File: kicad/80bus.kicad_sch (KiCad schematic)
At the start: 9 parts, among them IC2 4049

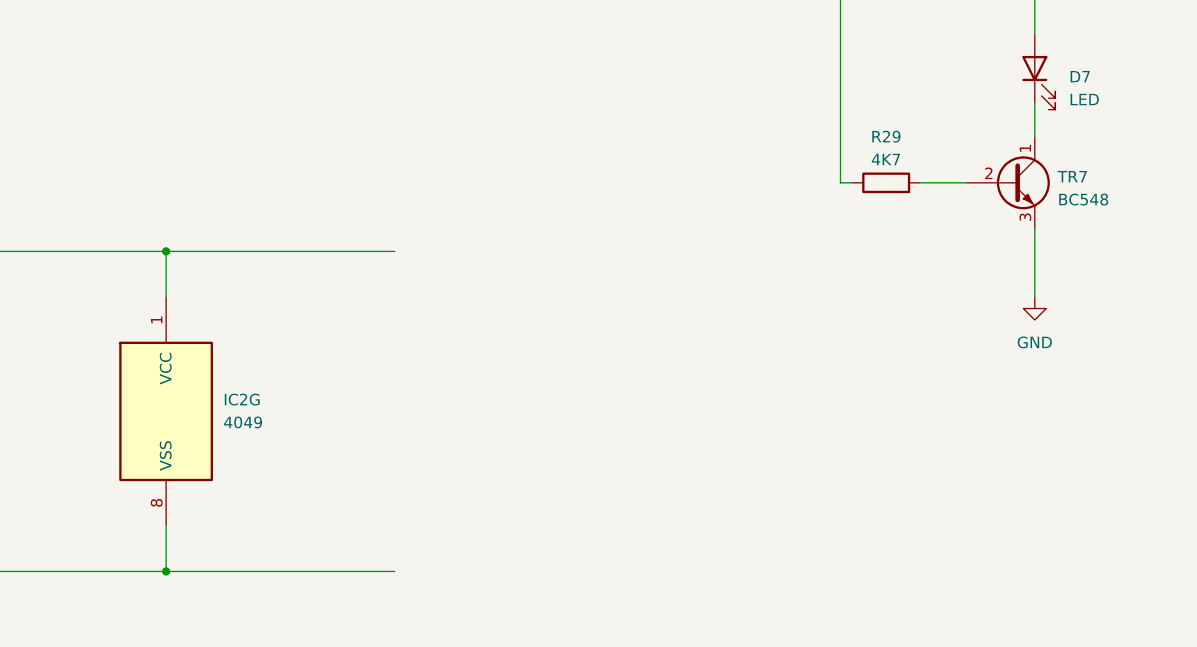
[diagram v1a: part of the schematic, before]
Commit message: Kicad 9 and Docs
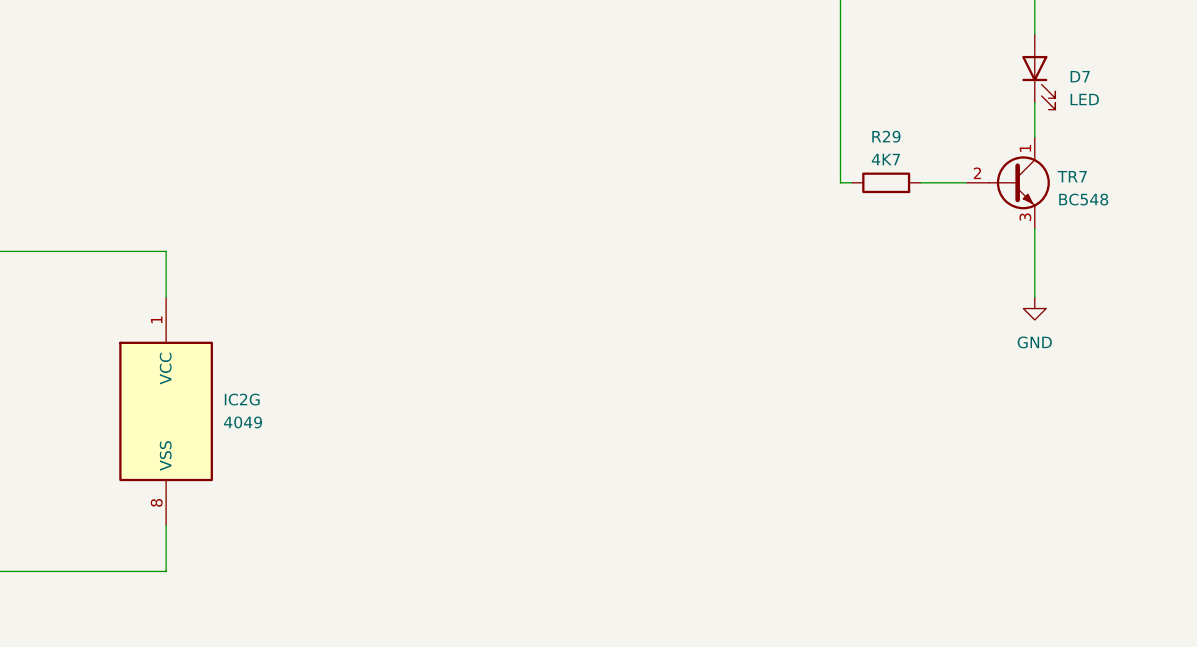
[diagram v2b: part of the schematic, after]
